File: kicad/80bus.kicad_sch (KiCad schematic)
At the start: 10 parts, among them J1 Conn_01x80, J2 Conn_01x80, J3 Conn_01x80, J4 Conn_01x80, J5 Conn_01x80, J6 Conn_01x80, SW1 Reset, T1 Terminal_01x05

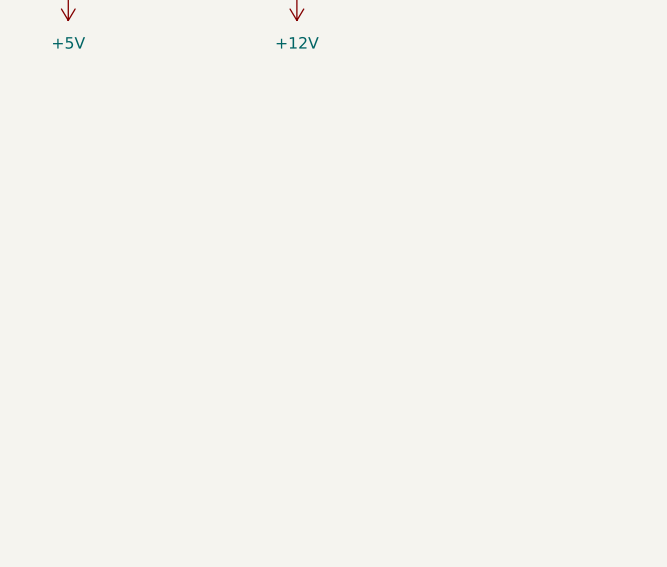
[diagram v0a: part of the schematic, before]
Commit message: Add mounting holes
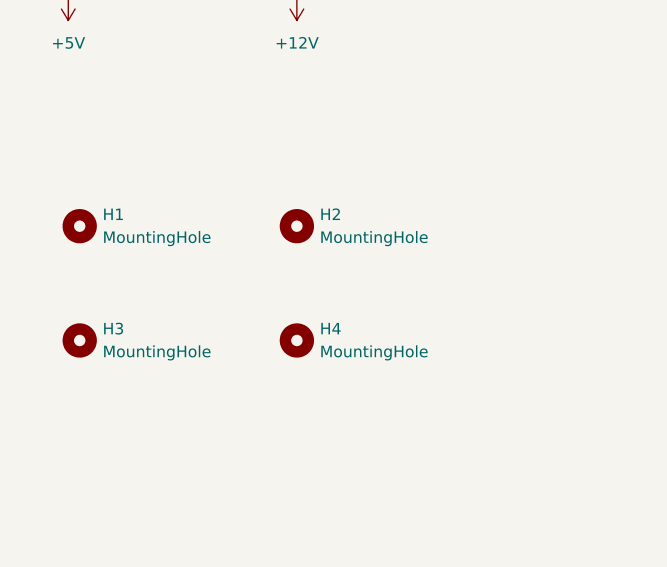
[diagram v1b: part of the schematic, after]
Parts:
- added H1, H2, H3, H4: MountingHole, MountingHole:MountingHole_3.5mm, symbol Mechanical:MountingHole
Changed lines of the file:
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@@
   (title_block
     (title "80-Bus Card Backplane")
-    (date "2023-03-04")
-    (rev "1.2.0")
+    (date "2024-06-22")
+    (rev "1.3.0")
   )
   (junction (at 201.93 200.66) (diameter 0) (color 0 0 0 0)
@@
     (stroke (width 0) (type default))
   )
+  (symbol (lib_id "Mechanical:MountingHole") (at 101.6 165.1 0) (unit 1)
+    (in_bom yes) (on_board yes) (dnp no) (fields_autoplaced)
+    (property "Reference" "H4" (at 104.14 163.83 0)
+      (effects (font (size 1.27 1.27)) (justify left))
+    )
+    (property "Value" "MountingHole" (at 104.14 166.37 0)
+      (effects (font (size 1.27 1.27)) (justify left))
+    )
+    (property "Footprint" "MountingHole:MountingHole_3.5mm" (at 101.6 165.1 0)
+      (effects (font (size 1.27 1.27)) hide)
+    )
+    (property "Datasheet" "~" (at 101.6 165.1 0)
+      (effects (font (size 1.27 1.27)) hide)
+    )
+    (instances
+      (project "80bus"
+        (path "/0bee0cad-d12c-495d-aa35-7d4ba8f05706"
+          (reference "H4") (unit 1)
+        )
+      )
+    )
+  )
   (symbol (lib_id "power:-5V") (at 264.16 226.06 180) (unit 1)
     (in_bom yes) (on_board yes) (dnp no) (fields_autoplaced)
@@
     )
   )
+  (symbol (lib_id "Mechanical:MountingHole") (at 77.47 165.1 0) (unit 1)
+    (in_bom yes) (on_board yes) (dnp no) (fields_autoplaced)
+    (property "Reference" "H3" (at 80.01 163.83 0)
+      (effects (font (size 1.27 1.27)) (justify left))
+    )
+    (property "Value" "MountingHole" (at 80.01 166.37 0)
+      (effects (font (size 1.27 1.27)) (justify left))
+    )
+    (property "Footprint" "MountingHole:MountingHole_3.5mm" (at 77.47 165.1 0)
+      (effects (font (size 1.27 1.27)) hide)
+    )
+    (property "Datasheet" "~" (at 77.47 165.1 0)
+      (effects (font (size 1.27 1.27)) hide)
+    )
+    (instances
+      (project "80bus"
+        (path "/0bee0cad-d12c-495d-aa35-7d4ba8f05706"
+          (reference "H3") (unit 1)
+        )
+      )
+    )
+  )
   (symbol (lib_id "Connector:Screw_Terminal_01x05") (at 276.86 238.76 0) (unit 1)
     (in_bom yes) (on_board yes) (dnp no) (fields_autoplaced)
@@
     )
   )
+  (symbol (lib_id "Mechanical:MountingHole") (at 101.6 152.4 0) (unit 1)
+    (in_bom yes) (on_board yes) (dnp no) (fields_autoplaced)
+    (property "Reference" "H2" (at 104.14 151.13 0)
+      (effects (font (size 1.27 1.27)) (justify left))
+    )
+    (property "Value" "MountingHole" (at 104.14 153.67 0)
+      (effects (font (size 1.27 1.27)) (justify left))
+    )
+    (property "Footprint" "MountingHole:MountingHole_3.5mm" (at 101.6 152.4 0)
+      (effects (font (size 1.27 1.27)) hide)
+    )
+    (property "Datasheet" "~" (at 101.6 152.4 0)
+      (effects (font (size 1.27 1.27)) hide)
+    )
+    (instances
+      (project "80bus"
+        (path "/0bee0cad-d12c-495d-aa35-7d4ba8f05706"
+          (reference "H2") (unit 1)
+        )
+      )
+    )
+  )
   (symbol (lib_id "power:+5V") (at 264.16 248.92 180) (unit 1)
     (in_bom yes) (on_board yes) (dnp no) (fields_autoplaced)
@@
         )
       )
+    )
+  )
+  (symbol (lib_id "Mechanical:MountingHole") (at 77.47 152.4 0) (unit 1)
+    (in_bom yes) (on_board yes) (dnp no) (fields_autoplaced)
+    (property "Reference" "H1" (at 80.01 151.13 0)
+      (effects (font (size 1.27 1.27)) (justify left))
+    )
+    (property "Value" "MountingHole" (at 80.01 153.67 0)
+      (effects (font (size 1.27 1.27)) (justify left))
+    )
+    (property "Footprint" "MountingHole:MountingHole_3.5mm" (at 77.47 152.4 0)
+      (effects (font (size 1.27 1.27)) hide)
+    )
+    (property "Datasheet" "~" (at 77.47 152.4 0)
+      (effects (font (size 1.27 1.27)) hide)
+    )
+    (instances
+      (project "80bus"
+        (path "/0bee0cad-d12c-495d-aa35-7d4ba8f05706"
+          (reference "H1") (unit 1)
+        )
+      )

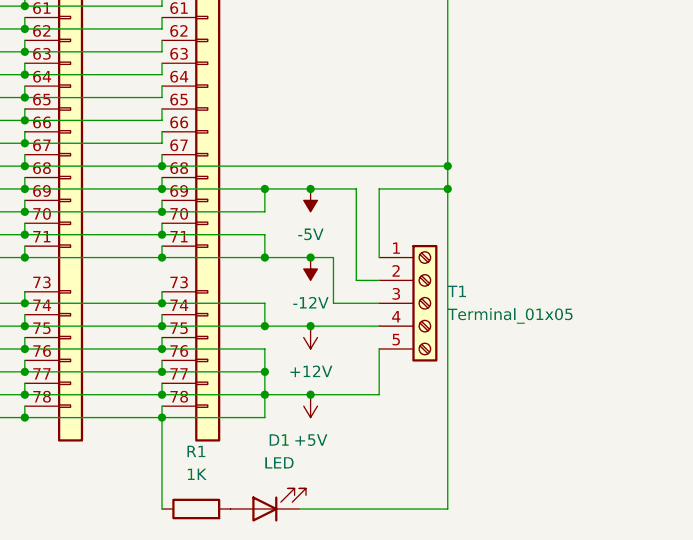
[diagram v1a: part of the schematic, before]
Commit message: Kicad, enhanced power, moved mount holes
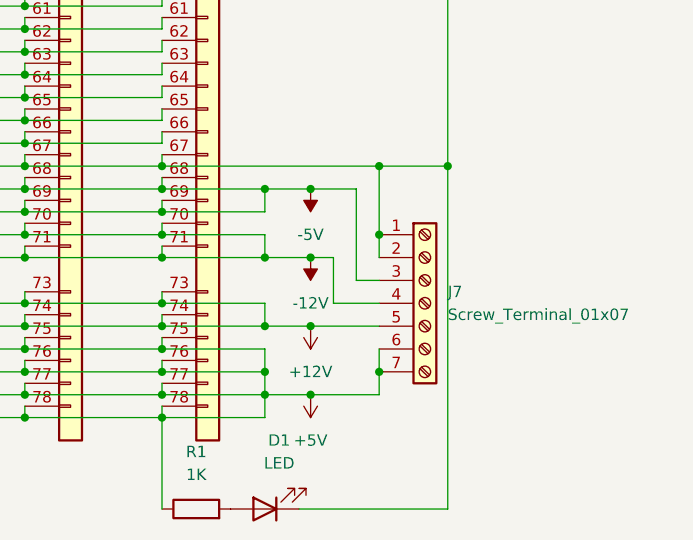
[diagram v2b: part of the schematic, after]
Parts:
- removed T1: Terminal_01x05, Connector_Molex:Molex_KK-396_5273-05A_1x05_P3.96mm_Vertical, symbol Connector:Screw_Terminal_01x05
- added J7: Screw_Terminal_01x07, Connector_Molex:Molex_KK-396_5273-07A_1x07_P3.96mm_Vertical, symbol Connector:Screw_Terminal_01x07
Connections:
- net +12V: now also J7.5 (Pin_5)
- net +5V: now also J7.6 (Pin_6), J7.7 (Pin_7)
- net -12V: now also J7.4 (Pin_4)
- net -5V: now also J7.3 (Pin_3)
- net GND: now also J7.1 (Pin_1), J7.2 (Pin_2)

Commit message: Kicad 9 and Docs
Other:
- title: 80-Bus Card Backplane -> 80-Bus Card Backplane - Kicad 9
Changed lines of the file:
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@@
 (kicad_sch
-	(version 20231120)
+	(version 20250114)
 	(generator "eeschema")
-	(generator_version "8.0")
+	(generator_version "9.0")
 	(paper "A3")
 	(title_block
-		(title "80-Bus Card Backplane")
-		(date "2024-06-22")
-		(rev "1.3.0")
+		(title "80-Bus Card Backplane - Kicad 9")
+		(date "2025-04-21")
+		(rev "1.5.0")
 	)
 	(junction
@@
 			)
 		)
-		(property "Description" ""
+		(property "Description" "Mounting Hole without connection"
 			(at 101.6 165.1 0)
 			(effects
@@
 			)
 		)
-		(property "Description" ""
+		(property "Description" "Power symbol creates a global label with name \"-5V\""
 			(at 264.16 226.06 0)
 			(effects
@@
 			)
 		)
-		(property "Description" ""
+		(property "Description" "Generic connector, single row, 01x78, script generated (kicad-library-utils/schlib/autogen/connector/)"
 			(at 177.8 254 0)
 			(effects
@@
 			)
 		)
-		(property "Description" ""
+		(property "Description" "Special symbol for telling ERC where power comes from"
 			(at 101.6 101.6 0)
 			(effects
@@
 			)
 		)
-		(property "Description" ""
+		(property "Description" "Power symbol creates a global label with name \"+12V\""
 			(at 101.6 127 0)
 			(effects
@@
 			)
 		)
-		(property "Description" ""
+		(property "Description" "Power symbol creates a global label with name \"GND\" , ground"
 			(at 264.16 63.5 0)
 			(effects
@@
 			)
 		)
-		(property "Description" ""
+		(property "Description" "Power symbol creates a global label with name \"+5V\""
 			(at 76.2 127 0)
 			(effects
@@
 			)
 		)
-		(property "Description" ""
+		(property "Description" "Power symbol creates a global label with name \"-12V\""
 			(at 264.16 233.68 0)
 			(effects
@@
 			)
 		)
-		(property "Description" ""
+		(property "Description" "Power symbol creates a global label with name \"-5V\""
 			(at 76.2 101.6 0)
 			(effects
@@
 			)
 		)
-		(property "Description" ""
+		(property "Description" "Special symbol for telling ERC where power comes from"
 			(at 76.2 127 0)
 			(effects
@@
 			)
 		)
-		(property "Description" ""
+		(property "Description" "Generic connector, single row, 01x78, script generated (kicad-library-utils/schlib/autogen/connector/)"
 			(at 193.04 254 0)
 			(effects
@@
 			)
 		)
-		(property "Description" ""
+		(property "Description" "Push button switch, generic, two pins"
 			(at 264.16 78.74 0)
 			(effects
@@
 			)
 		)
-		(property "Description" ""
+		(property "Description" "Power symbol creates a global label with name \"-12V\""
 			(at 101.6 101.6 0)
 			(effects
@@
 			)
 		)
-		(property "Description" ""
+		(property "Description" "Mounting Hole without connection"
 			(at 77.47 165.1 0)
 			(effects
@@
 			)
 		)
-		(property "Description" ""
+		(property "Description" "Power symbol creates a global label with name \"GND\" , ground"
 			(at 88.9 111.76 0)
 			(effects
@@
 			)
 		)
-		(property "Description" ""
+		(property "Description" "Generic connector, single row, 01x78, script generated (kicad-library-utils/schlib/autogen/connector/)"
 			(at 223.52 254 0)
 			(effects
@@
 			)
 		)
-		(property "Description" ""
+		(property "Description" "Special symbol for telling ERC where power comes from"
 			(at 101.6 127 0)
 			(effects
@@
 			)
 		)
-		(property "Description" ""
+		(property "Description" "Light emitting diode"
+			(at 259.08 261.62 0)
+			(effects
+				(font
+					(size 1.27 1.27)
+				)
+				(hide yes)
+			)
+		)
+		(property "Sim.Pins" "1=K 2=A"
 			(at 259.08 261.62 0)
 			(effects
@@
 			)
 		)
-		(property "Description" ""
+		(property "Description" "Generic connector, single row, 01x78, script generated (kicad-library-utils/schlib/autogen/connector/)"
 			(at 254 254 0)
 			(effects
@@
 			)
 		)
-		(property "Description" ""
+		(property "Description" "Generic connector, single row, 01x78, script generated (kicad-library-utils/schlib/autogen/connector/)"
 			(at 238.76 254 0)
 			(effects
@@
 			)
 		)
-		(property "Description" ""
+		(property "Description" "Mounting Hole without connection"
 			(at 101.6 152.4 0)
 			(effects
@@
 			)
 		)
-		(property "Description" ""
+		(property "Description" "Power symbol creates a global label with name \"+5V\""
 			(at 264.16 248.92 0)
 			(effects
@@
 			)
 		)
-		(property "Description" ""
+		(property "Description" "Power symbol creates a global label with name \"+12V\""
 			(at 264.16 241.3 0)
 			(effects
@@
 			)
 		)
-		(property "Description" ""
+		(property "Description" "Mounting Hole without connection"
 			(at 77.47 152.4 0)
 			(effects
@@
 			)
 		)
-		(property "Description" ""
+		(property "Description" "Resistor"
 			(at 251.46 261.62 0)
 			(effects
@@
 			)
 		)
-		(property "Description" ""
+		(property "Description" "Special symbol for telling ERC where power comes from"
 			(at 76.2 101.6 0)
 			(effects
@@
 			)
 		)
-		(property "Description" ""
+		(property "Description" "Generic connector, single row, 01x78, script generated (kicad-library-utils/schlib/autogen/connector/)"
 			(at 208.28 254 0)
 			(effects
@@
 			)
 		)
-		(property "Description" ""
+		(property "Description" "Special symbol for telling ERC where power comes from"
 			(at 88.9 111.76 0)
 			(effects
@@
 		)
 	)
+	(embedded_fonts no)
 )
